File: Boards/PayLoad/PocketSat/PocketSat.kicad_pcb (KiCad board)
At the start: 4 copper layers, 45.5 x 45.5 mm, 82 parts, among them J20 DX07S016JA1R1500, J3 MEM2061-01-188-00-A_REVA, J5 BM03B-SRSS-TBLFSN, Q1 BC857CMB_315, U1 HDC2080DMBR, U4 LPS22DFTR, U5 W25Q128JVSIQ TR, U6 BMP581, U8 ST1L05APU33R

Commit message: PocketStat Ground Planes Update
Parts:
- removed the G*** at (143.2, 68.0)
- added G***: LOGO, PocketSat-text:PocketSat_txt, F.Cu at (142.8, 68.0)
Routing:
- net GND: vias 176 -> 208

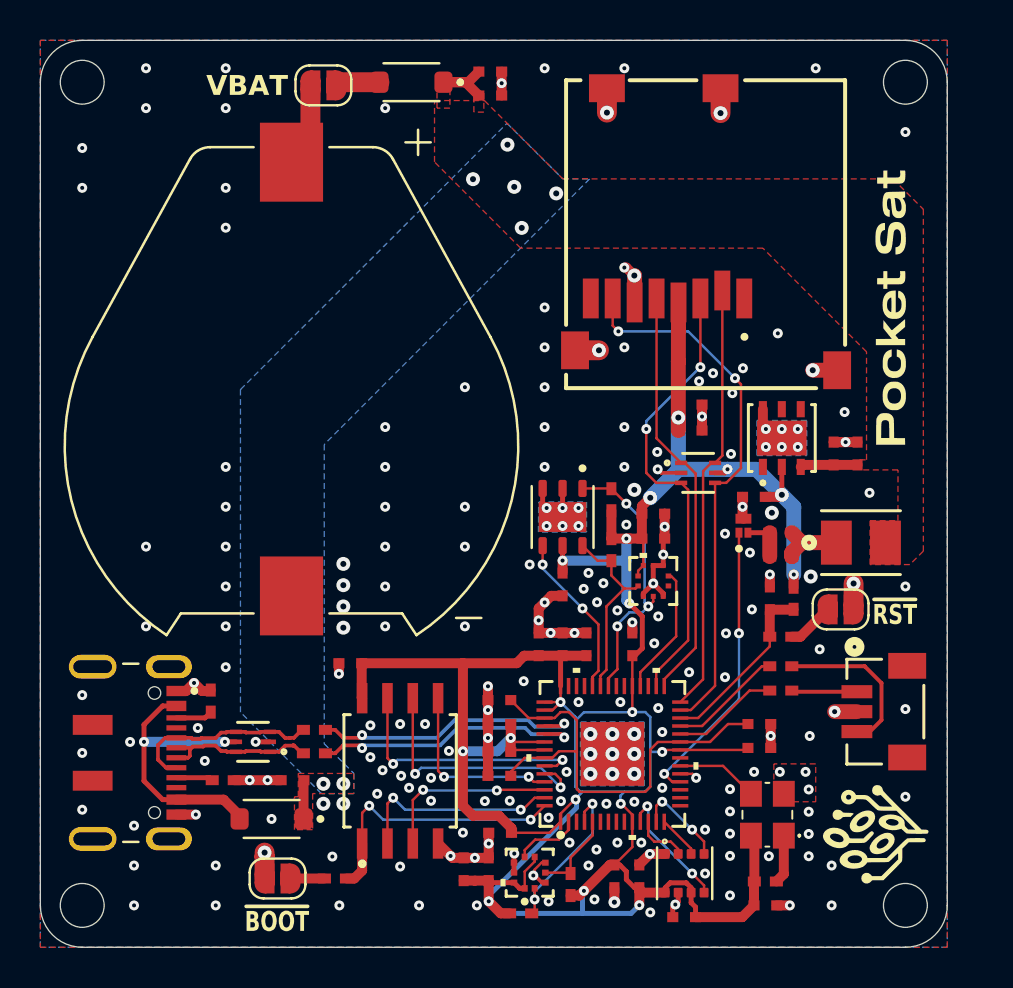
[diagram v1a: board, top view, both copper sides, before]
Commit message: Adicionei um driver novo de leds e outras correçoes
Adicionei um novo driver de leds substitui pelo velho e corrigimos mais
erros de DRC
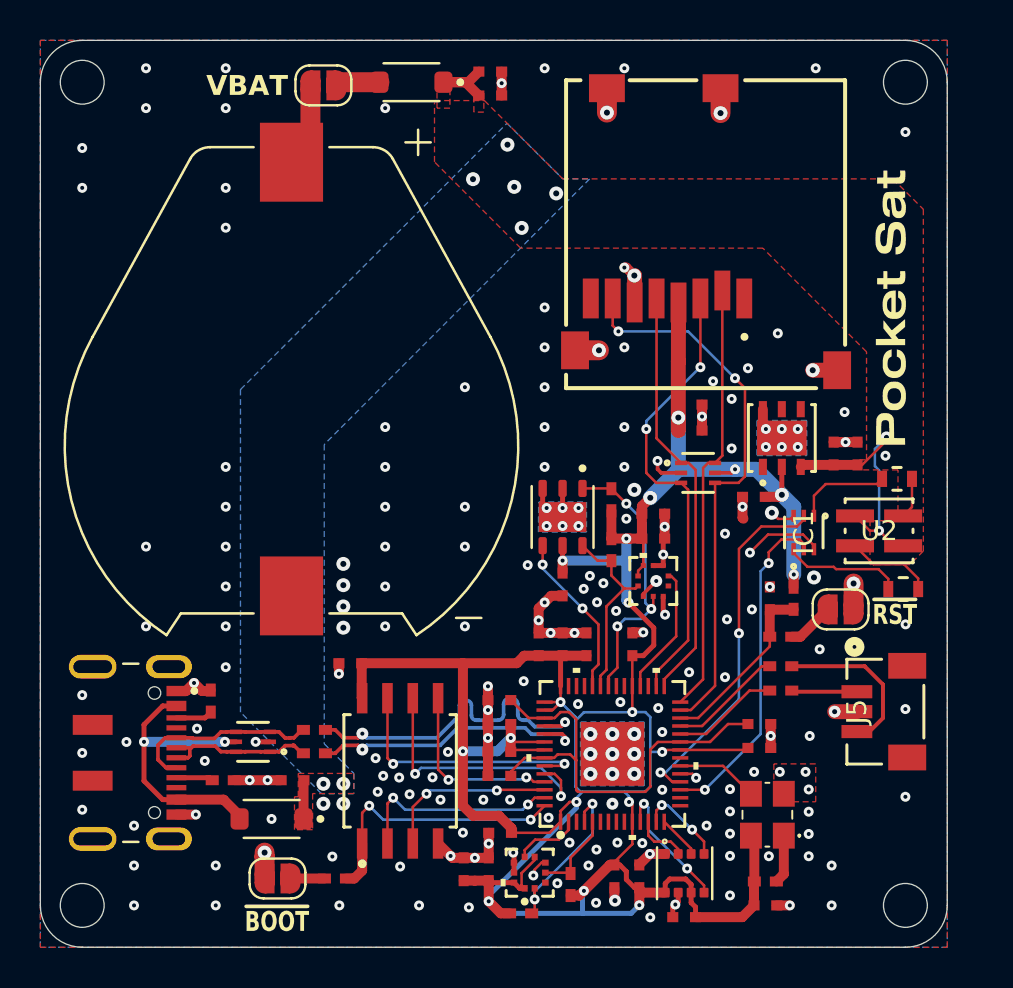
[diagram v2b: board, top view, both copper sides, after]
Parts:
- removed CR1: VLMC3100-GS08, LED-Green_VLMC3100-GS08:LED_PLCC_VSMB
- removed the G*** at (141.9, 94.3)
- removed Q1: BC857CMB_315, PNP_BC857CMB_315:TRANS_PMZB550UNEYL
- removed R20: 1k, Resistor-0402:RES_0402
- removed R21: 2k, Resistor-0402:RES_0402
- added G***: LOGO, PocketSat:PocketSatLogo, B.Cu at (139.5, 92.2)
- added IC1: NSVT30010MXV6T1G, 2 PNP:SOT-563_1P3X1P7_ONS, F.Cu at (138.3, 79.2)
- added R4: 100, Resistor-0603:RES_0603, F.Cu at (143.3, 82.0)
- added R5: 100, Resistor-0603:RES_0603, F.Cu at (143.0, 76.5)
- added U2: VLMKG3400-GS08, VLMKG3400-GS08:SMT_00-GS08_VIS, F.Cu at (142.1, 79.1)
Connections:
- J5 pad 4: (no net) -> GND
- J5 pad 5: (no net) -> GND
- MCU2 pad 17: unconnected-(MCU2-GPIO14-Pad17) -> /Green Status
- MCU2 pad 18: /LED Status -> /Red Status
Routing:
- net /Red Status: track 0.00 -> 18.2 mm, vias 0 -> 2
- net /Green Status: track 0.00 -> 17.1 mm, vias 0 -> 2
- net /LED Status: track 14.6 -> 0.00 mm, vias 2 -> 0
- net +5V: track 8.87 -> 19.0 mm, vias 7 -> 9
- net Net-(IC1-E2): track 0.00 -> 5.98 mm
- net Net-(IC1-E1): track 0.00 -> 4.78 mm
- net Net-(U2-A_Green): track 0.00 -> 4.38 mm
- net GND: track 56.9 -> 61.2 mm, vias 208 -> 198
- net Net-(CR1-Pad1): track 3.35 -> 0.00 mm
- net /D-: track 13.6 -> 17.0 mm
- net Net-(Q1-Pad2): track 2.32 -> 0.00 mm
- net Net-(U2-A_Red): track 0.00 -> 2.04 mm
- net +3.3V: track 151.6 -> 153.2 mm
- net /MCU SCLK SPI: track 13.0 -> 13.9 mm
- net /D+: track 13.7 -> 14.4 mm
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
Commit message: Correção DFM JLC
Modifiquei a PCB para passar em todos os criterios da JLC DFM
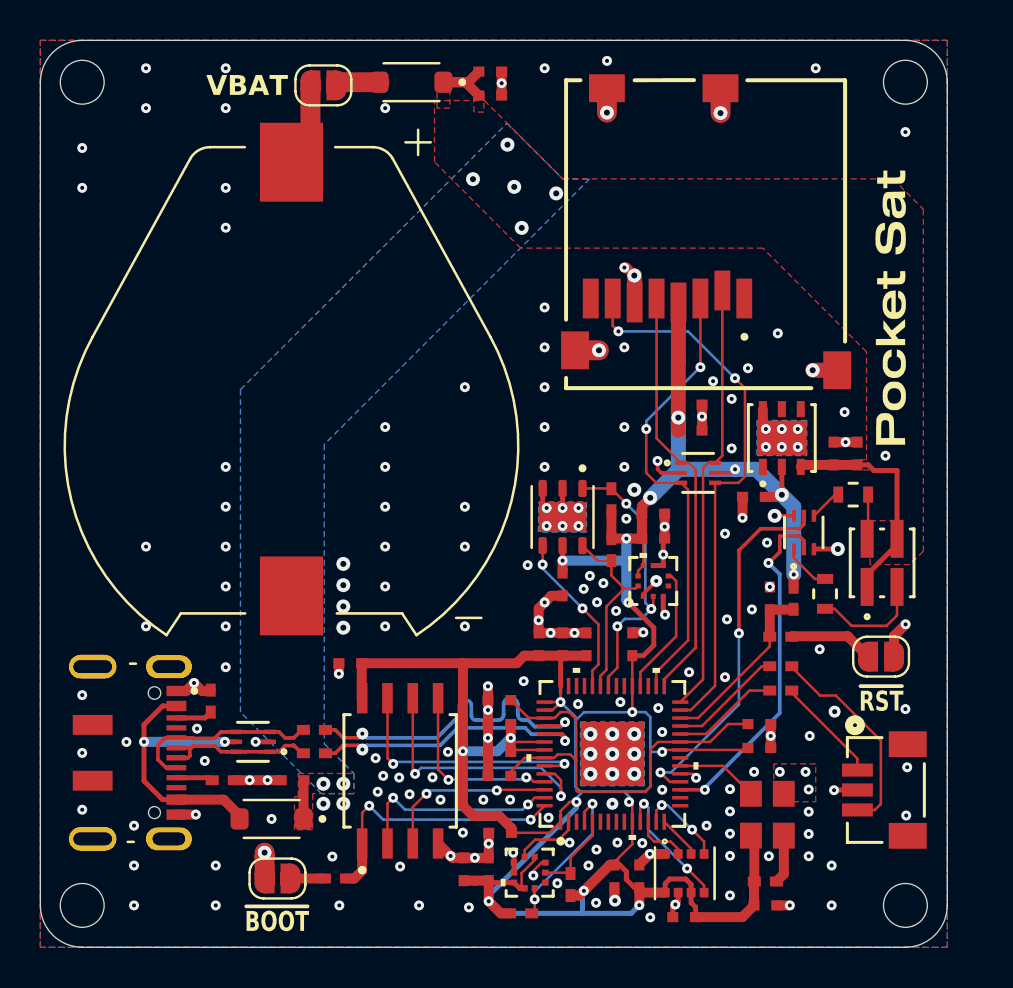
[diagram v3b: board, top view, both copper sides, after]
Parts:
- removed the G*** at (134.1, 74.5)
- removed the G*** at (132.8, 90.3)
- removed the G*** at (123.5, 78.5)
- HM1: value BME280 -> PSON65P250X250X100-8N
- moved J5 3.93 mm to (142.4, 92.1)
- moved R4 3.93 mm to (139.4, 82.3), turned to 90 degrees
- moved JP5 3.12 mm to (142.2, 85.4)
- moved R5 2.34 mm to (140.8, 77.3)
- moved U2 1.61 mm to (142.2, 80.7), turned to 90 degrees
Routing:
- net Net-(IC1-E2): track 5.98 -> 2.44 mm
- net Net-(IC1-E1): track 4.78 -> 1.66 mm
- net GND: track 61.2 -> 58.1 mm, vias 198 -> 199
- net /SWD: track 8.23 -> 10.5 mm
- net /CLK SWD: track 3.21 -> 5.35 mm
- net /MCU ~{RST}: track 2.37 -> 4.26 mm
- net +5V: track 19.0 -> 17.4 mm, vias 9 -> 7
- net Net-(U2-A_Green): track 4.38 -> 5.61 mm
- net /Green Status: track 17.1 -> 17.7 mm

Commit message: Modifiquei as footprints
Modifiquei as footprints dos condensadores e resistencias para dar mais
estabilidade.
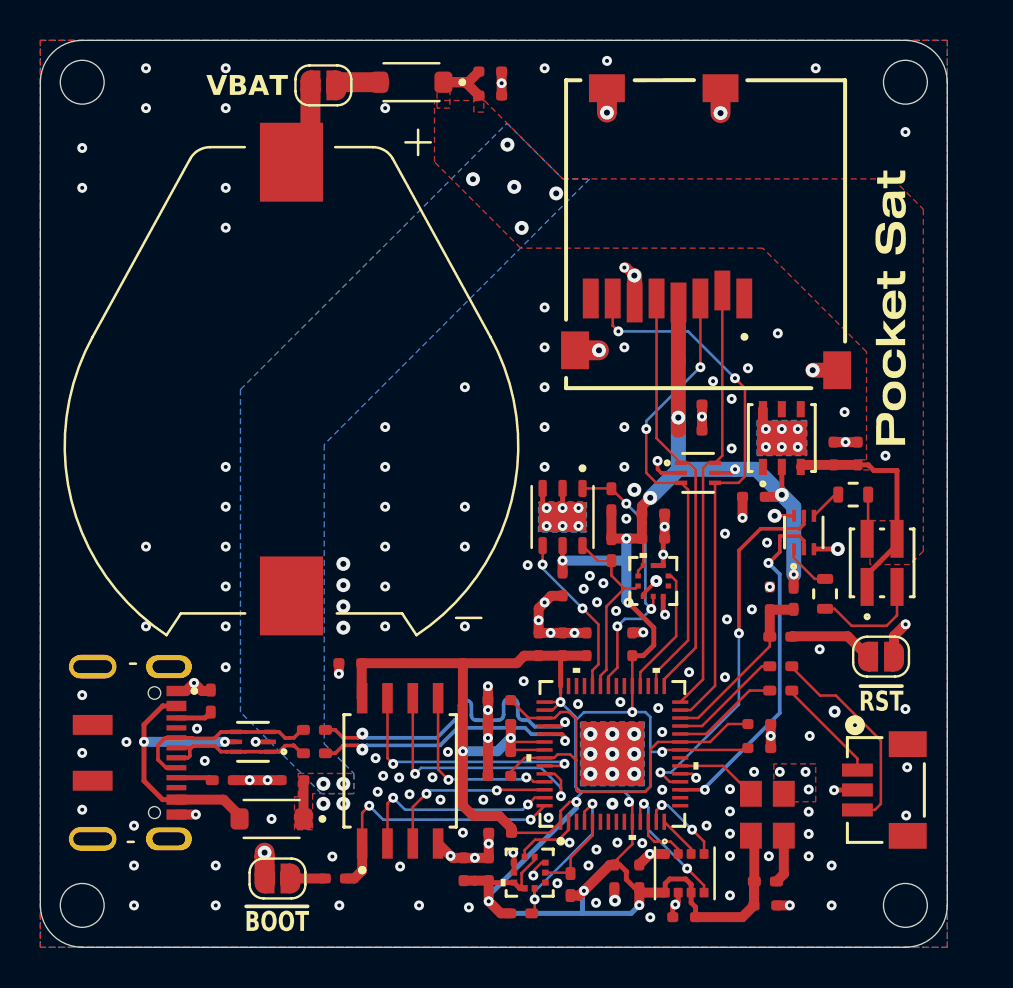
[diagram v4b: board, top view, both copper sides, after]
